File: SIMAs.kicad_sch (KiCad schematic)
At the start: 10 parts, among them J10 Conn_01x02_Pin, J3 Conn_01x04_Socket, J4 Conn_01x04_Socket, J5 Conn_01x04_Socket, J6 Conn_01x03_Socket, J9 Conn_01x03_Socket, U1 mini_esp32

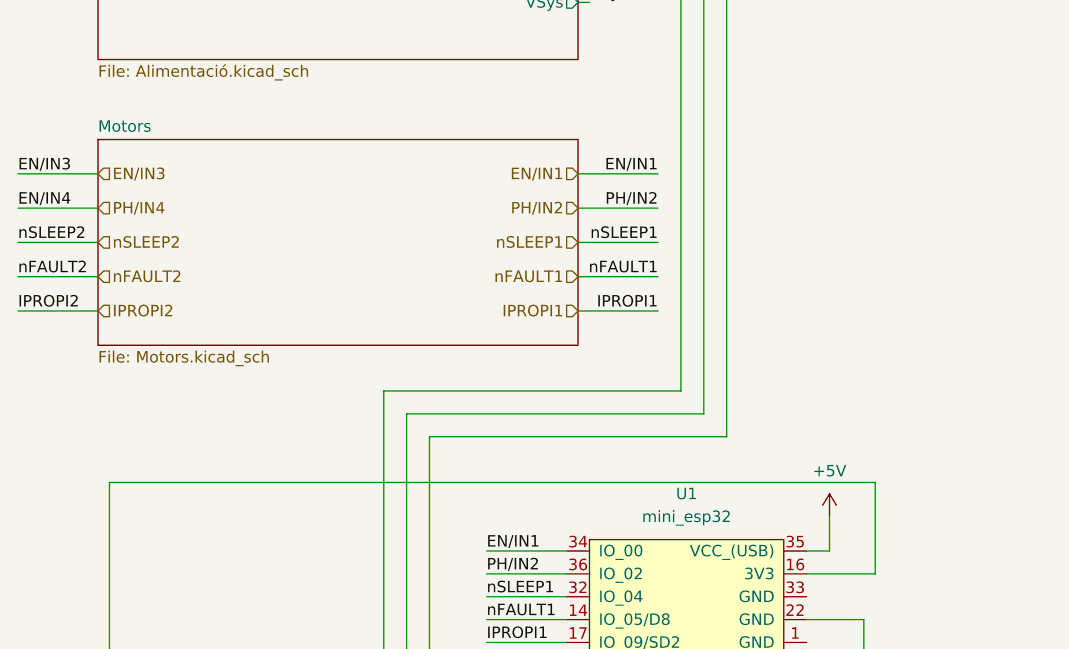
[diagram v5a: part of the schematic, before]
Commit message: Pistes
S'han fet les pistes i les connexions entre tots els components. Falta revisar-les.
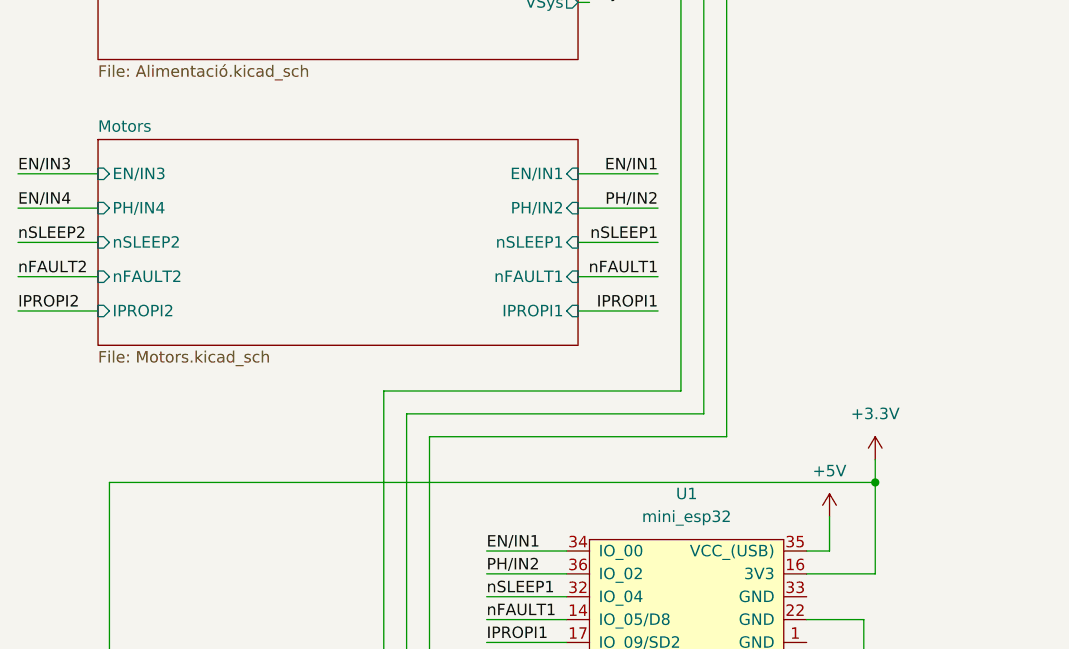
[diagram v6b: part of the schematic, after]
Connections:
- net +3.3V: now also R28.2, R29.2, R30.2, U1.16 (3V3)
- net PH/IN4 renamed EN/IN4
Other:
- sheet Motors ports: added EN/IN1, EN/IN3, IPROPI1, IPROPI2, PH/IN2, PH/IN4, nFAULT1, nFAULT2, nSLEEP1, nSLEEP2; removed none
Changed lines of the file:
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@@
+	)
+	(junction
+		(at 118.11 99.06)
+		(diameter 0)
+		(color 0 0 0 0)
 	)
 	(junction
@@
 	(wire
 		(pts
+			(xy 118.11 96.52) (xy 118.11 99.06)
+		)
+		(stroke
+			(width 0)
+			(type default)
+		)
+	)
+	(wire
+		(pts
 			(xy 110.49 109.22) (xy 118.11 109.22)
 		)
@@
 				(hide yes)
 			)
-		)
-	)
-	(hierarchical_label "EN{slash}IN1"
-		(shape input)
-		(at 85.09 64.77 180)
-		(fields_autoplaced yes)
-		(effects
-			(font
-				(size 1.27 1.27)
-			)
-			(justify right)
-		)
-	)
-	(hierarchical_label "nFAULT2"
-		(shape input)
-		(at 31.75 76.2 0)
-		(fields_autoplaced yes)
-		(effects
-			(font
-				(size 1.27 1.27)
-			)
-			(justify left)
-		)
-	)
-	(hierarchical_label "PH{slash}IN4"
-		(shape input)
-		(at 31.75 68.58 0)
-		(fields_autoplaced yes)
-		(effects
-			(font
-				(size 1.27 1.27)
-			)
-			(justify left)
-		)
-	)
-	(hierarchical_label "nFAULT1"
-		(shape input)
-		(at 85.09 76.2 180)
-		(fields_autoplaced yes)
-		(effects
-			(font
-				(size 1.27 1.27)
-			)
-			(justify right)
-		)
-	)
-	(hierarchical_label "PH{slash}IN2"
-		(shape input)
-		(at 85.09 68.58 180)
-		(fields_autoplaced yes)
-		(effects
-			(font
-				(size 1.27 1.27)
-			)
-			(justify right)
-		)
-	)
-	(hierarchical_label "nSLEEP1"
-		(shape input)
-		(at 85.09 72.39 180)
-		(fields_autoplaced yes)
-		(effects
-			(font
-				(size 1.27 1.27)
-			)
-			(justify right)
-		)
-	)
-	(hierarchical_label "IPROPI2"
-		(shape input)
-		(at 31.75 80.01 0)
-		(fields_autoplaced yes)
-		(effects
-			(font
-				(size 1.27 1.27)
-			)
-			(justify left)
-		)
-	)
-	(hierarchical_label "EN{slash}IN3"
-		(shape input)
-		(at 31.75 64.77 0)
-		(fields_autoplaced yes)
-		(effects
-			(font
-				(size 1.27 1.27)
-			)
-			(justify left)
-		)
-	)
-	(hierarchical_label "nSLEEP2"
-		(shape input)
-		(at 31.75 72.39 0)
-		(fields_autoplaced yes)
-		(effects
-			(font
-				(size 1.27 1.27)
-			)
-			(justify left)
-		)
-	)
-	(hierarchical_label "IPROPI1"
-		(shape input)
-		(at 85.09 80.01 180)
-		(fields_autoplaced yes)
-		(effects
-			(font
-				(size 1.27 1.27)
-			)
-			(justify right)
 		)
 	)
@@
 	)
 	(symbol
+		(lib_id "power:+3.3V")
+		(at 118.11 96.52 0)
+		(unit 1)
+		(exclude_from_sim no)
+		(in_bom yes)
+		(on_board yes)
+		(dnp no)
+		(fields_autoplaced yes)
+		(property "Reference" "#PWR023"
+			(at 118.11 100.33 0)
+			(effects
+				(font
+					(size 1.27 1.27)
+				)
+				(hide yes)
+			)
+		)
+		(property "Value" "+3.3V"
+			(at 118.11 91.44 0)
+			(effects
+				(font
+					(size 1.27 1.27)
+				)
+			)
+		)
+		(property "Footprint" ""
+			(at 118.11 96.52 0)
+			(effects
+				(font
+					(size 1.27 1.27)
+				)
+				(hide yes)
+			)
+		)
+		(property "Datasheet" ""
+			(at 118.11 96.52 0)
+			(effects
+				(font
+					(size 1.27 1.27)
+				)
+				(hide yes)
+			)
+		)
+		(property "Description" "Power symbol creates a global label with name \"+3.3V\""
+			(at 118.11 96.52 0)
+			(effects
+				(font
+					(size 1.27 1.27)
+				)
+				(hide yes)
+			)
+		)
+		(pin "1"
+		)
+		(instances
+			(project ""
+				(path "/0e086368-df4c-4139-a634-f31f7cd00dd9"
+					(reference "#PWR023")
+					(unit 1)
+				)
+			)
+		)
+	)
+	(symbol
 		(lib_id "ESP32_mini:mini_esp32")
 		(at 96.52 104.14 0)
@@
 			)
 		)
+		(pin "IPROPI2" input
+			(at 31.75 80.01 180)
+			(effects
+				(font
+					(size 1.27 1.27)
+				)
+				(justify left)
+			)
+		)
+		(pin "nFAULT2" input
+			(at 31.75 76.2 180)
+			(effects
+				(font
+					(size 1.27 1.27)
+				)
+				(justify left)
+			)
+		)
+		(pin "nSLEEP2" input
+			(at 31.75 72.39 180)
+			(effects
+				(font
+					(size 1.27 1.27)
+				)
+				(justify left)
+			)
+		)
+		(pin "nSLEEP1" input
+			(at 85.09 72.39 0)
+			(effects
+				(font
+					(size 1.27 1.27)
+				)
+				(justify right)
+			)
+		)
+		(pin "IPROPI1" input
+			(at 85.09 80.01 0)
+			(effects
+				(font
+					(size 1.27 1.27)
+				)
+				(justify right)
+			)
+		)
+		(pin "nFAULT1" input
+			(at 85.09 76.2 0)
+			(effects
+				(font
+					(size 1.27 1.27)
+				)
+				(justify right)
+			)
+		)
+		(pin "PH{slash}IN4" input
+			(at 31.75 68.58 180)
+			(effects
+				(font
+					(size 1.27 1.27)
+				)
+				(justify left)
+			)
+		)
+		(pin "EN{slash}IN3" input
+			(at 31.75 64.77 180)
+			(effects
+				(font
+					(size 1.27 1.27)
+				)
+				(justify left)
+			)
+		)
+		(pin "PH{slash}IN2" input
+			(at 85.09 68.58 0)
+			(effects
+				(font
+					(size 1.27 1.27)
+				)
+				(justify right)
+			)
+		)
+		(pin "EN{slash}IN1" input
+			(at 85.09 64.77 0)
+			(effects
+				(font
+					(size 1.27 1.27)
+				)
+				(justify right)
+			)
+		)

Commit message: Revisio de la placa
S'ha revisat la placa
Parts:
- added D3: WS2812B, LED_SMD:LED_WS2812B_PLCC4_5.0x5.0mm_P3.2mm, symbol LED:WS2812B
- added D4: D, Diode_SMD:D_SMA_Handsoldering, symbol Device:D
- added D7: 5 V, Diode_SMD:D_SOD-323, symbol Device:D_Zener
- added D8: 3,3 V, Diode_SMD:D_SOD-323, symbol Device:D_Zener
- added J11, J12: Conn_01x03_Pin, Connector_JST:JST_PH_B3B-PH-K_1x03_P2.00mm_Vertical, symbol Connector:Conn_01x03_Pin
- added J13: Conn_01x05_Pin, Connector_JST:JST_PH_B5B-PH-K_1x05_P2.00mm_Vertical, symbol Connector:Conn_01x05_Pin
- added R10: DNP, Resistor_SMD:R_0603_1608Metric, symbol Device:R
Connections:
- net nFAULT1 is gone; now on net EN/IN4: U1.14 (IO_05/D8)
- net nSLEEP1 is gone; now on net EN/IN3: U1.32 (IO_04)
- net nSLEEP2 is gone; now on net SONS1: U1.18 (IO_13/TCK)
- net +3.3V: now also D8.1 (K), J12.3 (Pin_3), J13.5 (Pin_5)
- net +5V: now also D4.2 (A), D7.1 (K), J11.3 (Pin_3)
- net ENC1: now also U1.12 (IO_23/D7); no longer U1.28 (IO_32)
- net ENC2: now also U1.26 (IO_25); no longer U1.9 (IO_33)
- net ENC3: now also U1.6 (IO_26/D0); no longer U1.11 (IO_34)
- net ENC4: now also U1.24 (IO_27); no longer U1.7 (IO_35)
- net EN/IN3: no longer U1.20 (IO_10/SD3)
- net EN/IN4: no longer U1.30 (IO_12/TDI)
- net GND: now also D3.3 (VSS), D7.2 (A), D8.2 (A), J11.1 (Pin_1), J12.1 (Pin_1), J13.1 (Pin_1)
- net IPROPI1: no longer U1.17 (IO_09/SD2)
- net IPROPI2: no longer U1.31 (IO_16/D4)
- net SERVO: now also U1.30 (IO_12/TDI); no longer U1.24 (IO_27)
- net SONS1: no longer U1.26 (IO_25)
- net SONS2: now also U1.13 (IO_14/TMS); no longer U1.6 (IO_26/D0)
- net LINIA3: now reaches U1.4 (IO_36/SVP/A0)
- net LINIA3: now also J13.2 (Pin_2)
- net EXT_GPIO: now reaches U1.8 (IO_18/D5)
- net EXT_GPIO: now also J12.2 (Pin_2)
- net nFAULT2 renamed Alimentació//INT
- net Alimentació//INT: no longer U1.13 (IO_14/TMS)
- new net: D3.2 (DOUT), J11.2 (Pin_2), R10.2
- new net: D3.1 (VDD), D4.1 (K)
- new net LEDs: D3.4 (DIN), R10.1, U1.31 (IO_16/D4)
- new net LINIA1: J13.4 (Pin_4), U1.11 (IO_34)
- new net LINIA2: J13.3 (Pin_3), U1.7 (IO_35)
- new net nFAULT: U1.9 (IO_33)
- new net nSLEEP: U1.28 (IO_32)
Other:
- note added: "GPIO"
- note added: "Proteccio ESD"
- note added: "Tira RGB"
- moved on the sheet: J10, J3, J4, J5, J6, J9

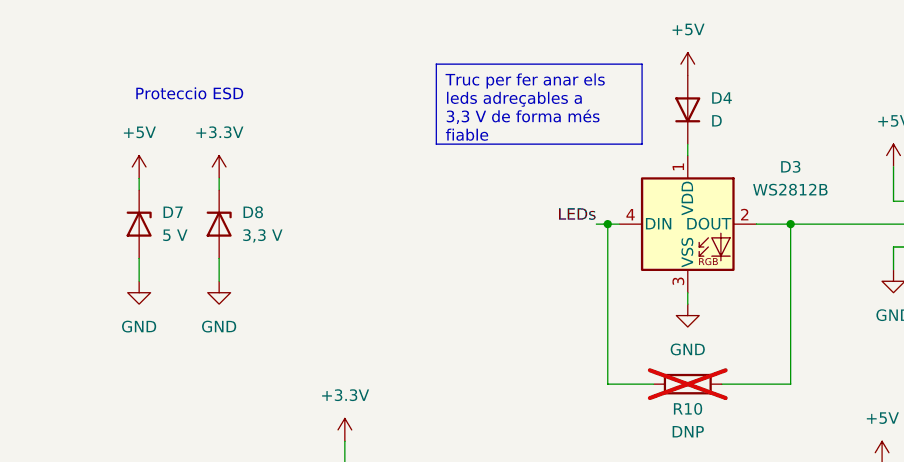
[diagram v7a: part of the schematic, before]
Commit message: Actualitzats valors dels components
S'han actualitzat els valors de components d'acord als comprats, s'ha canviat algun valor per conveniència, i s'ha acabat de donar valors a tots els components
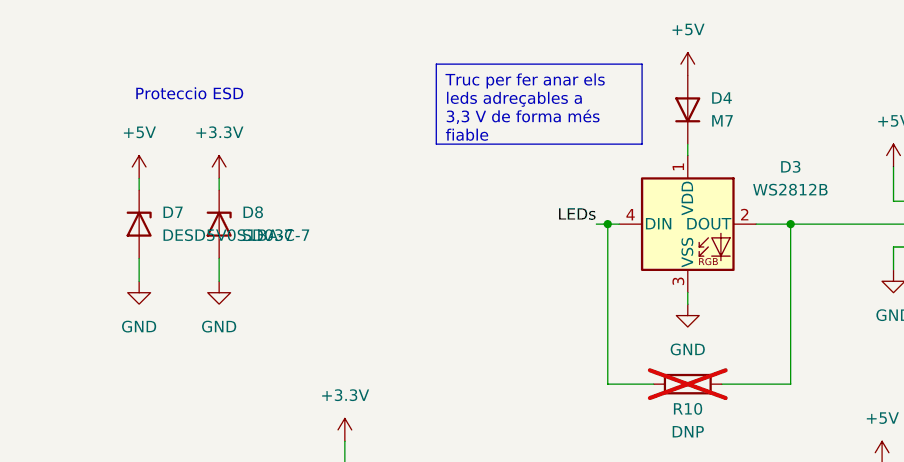
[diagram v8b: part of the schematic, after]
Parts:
- D4: value D -> M7
- D7: value 5 V -> DESD5V0S1BA-7
- D8: value 3,3 V -> SD03C-7
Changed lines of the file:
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@@
 	(label "nFAULT"
 		(at 22.86 76.2 0)
-		(fields_autoplaced yes)
 		(effects
 			(font
@@
 	(label "VSys"
 		(at 86.36 45.72 0)
-		(fields_autoplaced yes)
 		(effects
 			(font
@@
 	(label "EN{slash}IN4"
 		(at 80.01 114.3 180)
-		(fields_autoplaced yes)
 		(effects
 			(font
@@
 	(label "ENC4"
 		(at 80.01 167.64 180)
-		(fields_autoplaced yes)
 		(effects
 			(font
@@
 	(label "LINIA3"
 		(at 186.69 154.94 180)
-		(fields_autoplaced yes)
 		(effects
 			(font
@@
 	(label "EN{slash}IN1"
 		(at 80.01 106.68 180)
-		(fields_autoplaced yes)
 		(effects
 			(font
@@
 	(label "nSLEEP"
 		(at 93.98 72.39 180)
-		(fields_autoplaced yes)
 		(effects
 			(font
@@
 	(label "LINIA2"
 		(at 186.69 152.4 180)
-		(fields_autoplaced yes)
 		(effects
 			(font
@@
 	(label "PH{slash}IN2"
 		(at 93.98 68.58 180)
-		(fields_autoplaced yes)
 		(effects
 			(font
@@
 	(label "EXT_GPIO"
 		(at 240.03 152.4 180)
-		(fields_autoplaced yes)
 		(effects
 			(font
@@
 	(label "nSLEEP"
 		(at 80.01 139.7 180)
-		(fields_autoplaced yes)
 		(effects
 			(font
@@
 	(label "PH{slash}IN2"
 		(at 80.01 109.22 180)
-		(fields_autoplaced yes)
 		(effects
 			(font
@@
 	(label "ENC2"
 		(at 186.69 78.74 180)
-		(fields_autoplaced yes)
 		(effects
 			(font
@@
 	(label "VSys"
 		(at 240.03 123.19 180)
-		(fields_autoplaced yes)
 		(effects
 			(font
@@
 	(label "SONS1"
 		(at 184.15 121.92 180)
-		(fields_autoplaced yes)
 		(effects
 			(font
@@
 	(label "ENC1"
 		(at 80.01 160.02 180)
-		(fields_autoplaced yes)
 		(effects
 			(font
@@
 	(label "FIDECURSA"
 		(at 237.49 97.79 180)
-		(fields_autoplaced yes)
 		(effects
 			(font
@@
 	(label "SONS1"
 		(at 80.01 124.46 180)
-		(fields_autoplaced yes)
 		(effects
 			(font
@@
 	(label "IPROPI2"
 		(at 22.86 80.01 0)
-		(fields_autoplaced yes)
 		(effects
 			(font
@@
 	(label "IPROPI1"
 		(at 93.98 80.01 180)
-		(fields_autoplaced yes)
 		(effects
 			(font
@@
 	(label "EN{slash}IN3"
 		(at 80.01 111.76 180)
-		(fields_autoplaced yes)
 		(effects
 			(font
@@
 	(label "ENC3"
 		(at 80.01 165.1 180)
-		(fields_autoplaced yes)
 		(effects
 			(font
@@
 	(label "ENC1"
 		(at 186.69 76.2 180)
-		(fields_autoplaced yes)
 		(effects
 			(font
@@
 	(label "LINIA3"
 		(at 80.01 149.86 180)
-		(fields_autoplaced yes)
 		(effects
 			(font
@@
 	(label "nFAULT"
 		(at 80.01 142.24 180)
-		(fields_autoplaced yes)
 		(effects
 			(font
@@
 	(label "SONS2"
 		(at 184.15 124.46 180)
-		(fields_autoplaced yes)
 		(effects
 			(font
@@
 	(label "EN{slash}IN1"
 		(at 93.98 64.77 180)
-		(fields_autoplaced yes)
 		(effects
 			(font
@@
 	(label "LEDs"
 		(at 80.01 129.54 180)
-		(fields_autoplaced yes)
 		(effects
 			(font
@@
 	(label "SONS2"
 		(at 80.01 127 180)
-		(fields_autoplaced yes)
 		(effects
 			(font
@@
 	(label "SERVO"
 		(at 80.01 121.92 180)
-		(fields_autoplaced yes)
 		(effects
 			(font
@@
 	(label "EXT_GPIO"
 		(at 80.01 134.62 180)
-		(fields_autoplaced yes)
 		(effects
 			(font
@@
 	(label "FIDECURSA"
 		(at 80.01 137.16 180)
-		(fields_autoplaced yes)
 		(effects
 			(font
@@
 	(label "LINIA1"
 		(at 186.69 149.86 180)
-		(fields_autoplaced yes)
 		(effects
 			(font
@@
 	(label "ENC2"
 		(at 80.01 162.56 180)
-		(fields_autoplaced yes)
 		(effects
 			(font
@@
 	(label "LINIA1"
 		(at 80.01 144.78 180)
-		(fields_autoplaced yes)
 		(effects
 			(font
@@
 	(label "nFAULT"
 		(at 93.98 76.2 180)
-		(fields_autoplaced yes)
 		(effects
 			(font
@@
 	(label "ENC3"
 		(at 186.69 91.44 180)
-		(fields_autoplaced yes)
 		(effects
 			(font
@@
 	(label "nSLEEP"
 		(at 22.86 72.39 0)
-		(fields_autoplaced yes)
 		(effects
 			(font
@@
 	(label "LEDs"
 		(at 208.28 44.45 180)
-		(fields_autoplaced yes)
 		(effects
 			(font
@@
 	(label "ENC4"
 		(at 186.69 93.98 180)
-		(fields_autoplaced yes)
 		(effects
 			(font
@@
 	(label "EN{slash}IN3"
 		(at 22.86 64.77 0)
-		(fields_autoplaced yes)
 		(effects
 			(font
@@
 	(label "EN{slash}IN4"
 		(at 22.86 68.58 0)
-		(fields_autoplaced yes)
 		(effects
 			(font
@@
 	(label "LINIA2"
 		(at 80.01 147.32 180)
-		(fields_autoplaced yes)
 		(effects
 			(font
@@
 	(label "SERVO"
 		(at 238.76 76.2 180)
-		(fields_autoplaced yes)
 		(effects
 			(font
@@
 			)
 		)
-		(property "Value" "5 V"
+		(property "Value" "DESD5V0S1BA-7"
 			(at 160.02 45.7199 90)
 			(effects
@@
 			)
 		)
-		(property "Value" "D"
+		(property "Value" "M7"
 			(at 220.98 33.0199 90)
 			(effects
@@
 			)
 		)
-		(property "Value" "3,3 V"
+		(property "Value" "SD03C-7"
 			(at 168.91 45.7199 90)
 			(effects
